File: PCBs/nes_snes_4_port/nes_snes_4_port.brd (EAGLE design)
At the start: 72.9 x 73.2 mm, 45 parts, among them J5 RJ45, J6 RJ45, J7 RJ45, J8 RJ45, J9 RJ45-S-4, U1 74245, U10 MC74VHC1GT125, U2 MC74VHC1GT125, U3 MC74VHC1GT125, U4 MC74VHC1GT125, U5 MC74VHC1GT125, U7 MC74VHC1GT125, U8 MC74VHC1GT125, U9 MC74VHC1GT125

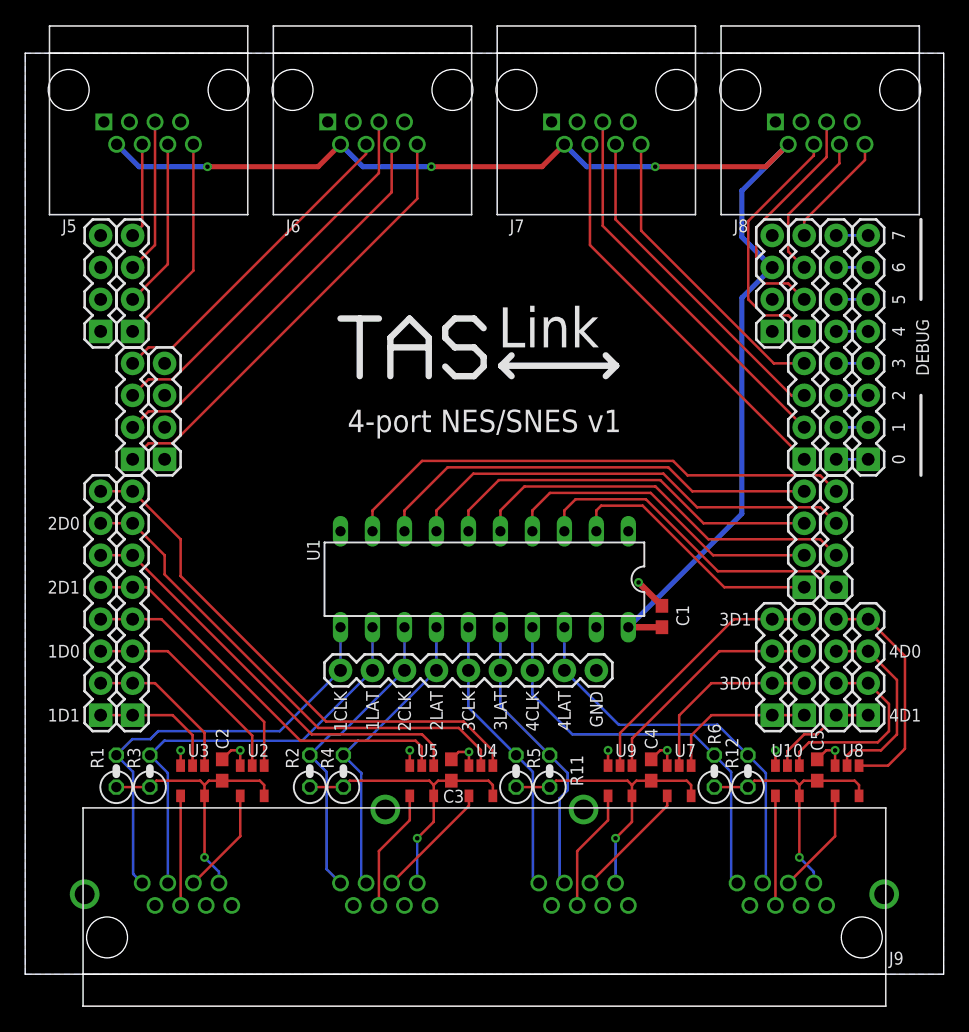
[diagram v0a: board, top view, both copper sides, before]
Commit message: NES/SNES 4-port PCB: Removed the power supply pins that did nothing. Fixed the backwards power supply pin. Added 4 ground tap pins.
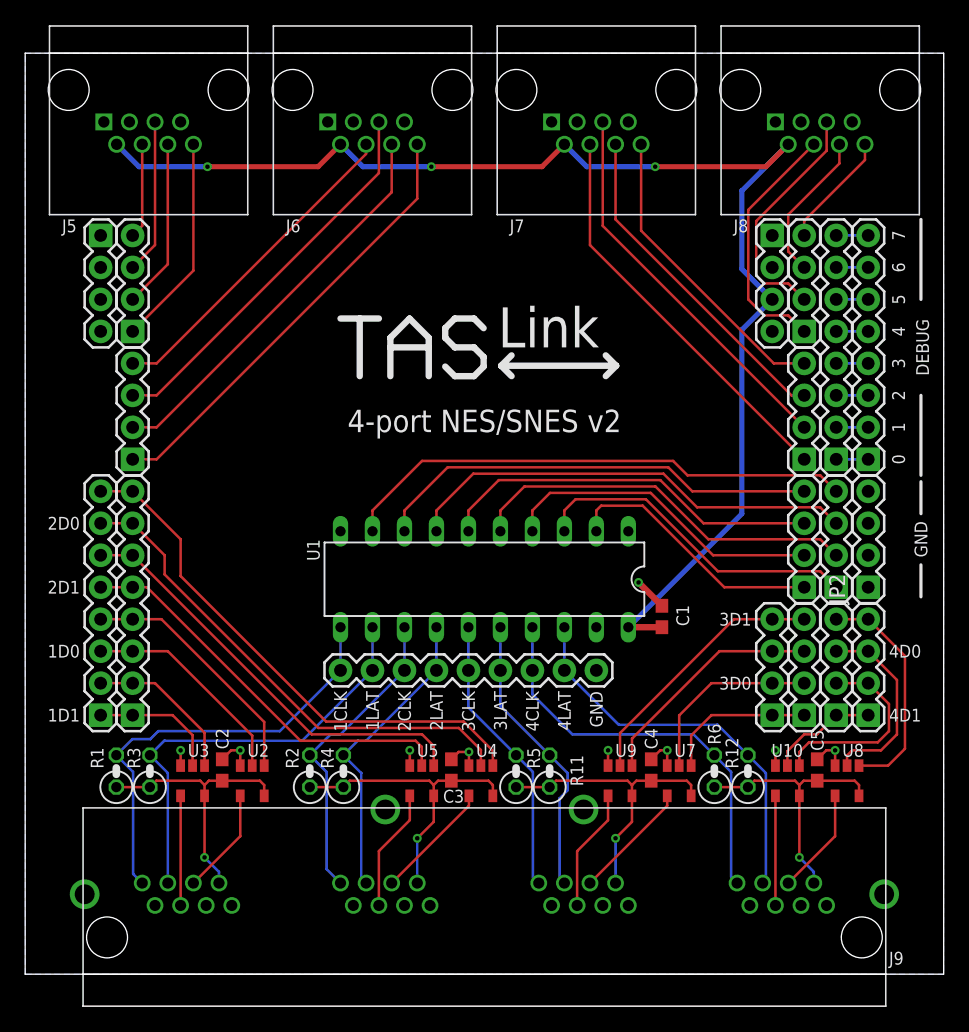
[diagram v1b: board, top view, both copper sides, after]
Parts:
- removed JP13: (no value), SparkFun-Connectors:1X04
- added JP2: (no value), SparkFun-Connectors:1X04
- moved JP1 7.62 mm to (6.35, 58.7), turned to 270 degrees
- moved JP12 7.62 mm to (59.7, 58.7), turned to 270 degrees
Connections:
- net GND: now also JP2.1, JP2.2, JP2.3, JP2.4; no longer JP13.1
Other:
- board text added: "4-port NES/SNES v2"
- board text removed: "4-port NES/SNES v1"
